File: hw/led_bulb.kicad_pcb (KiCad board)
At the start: 2 copper layers, 92.4 x 91.4 mm, 109 parts, among them P1 USB_OTG, P10 CONN_01X02, P11 CONN_01X02, P12 CONN_01X02, P13 CONN_01X02, P14 CONN_01X02, P15 CONN_01X02, P16 CONN_01X02, P17 CONN_01X02, P18 CONN_01X02, P19 CONN_01X02, P2 CONN_01X02, P20 CONN_01X02, P21 CONN_01X02, P22 CONN_01X02, P23 CONN_01X02, P24 CONN_01X02, P25 CONN_01X02, P26 CONN_01X02, P27 CONN_01X02, P28 CONN_01X02, P29 CONN_01X02, P3 CONN_01X02, P30 CONN_01X02, P31 CONN_01X02, P32 CONN_01X02, P33 CONN_01X02, P4 CONN_01X02, P5 CONN_01X02, P6 CONN_01X02, P7 CONN_01X02, P8 CONN_01X02, P9 CONN_01X02, SW1 SW_RST, SW2 SW_FLASH, U1 CP2102, U3 ESP-12E, U4 AP1117D33

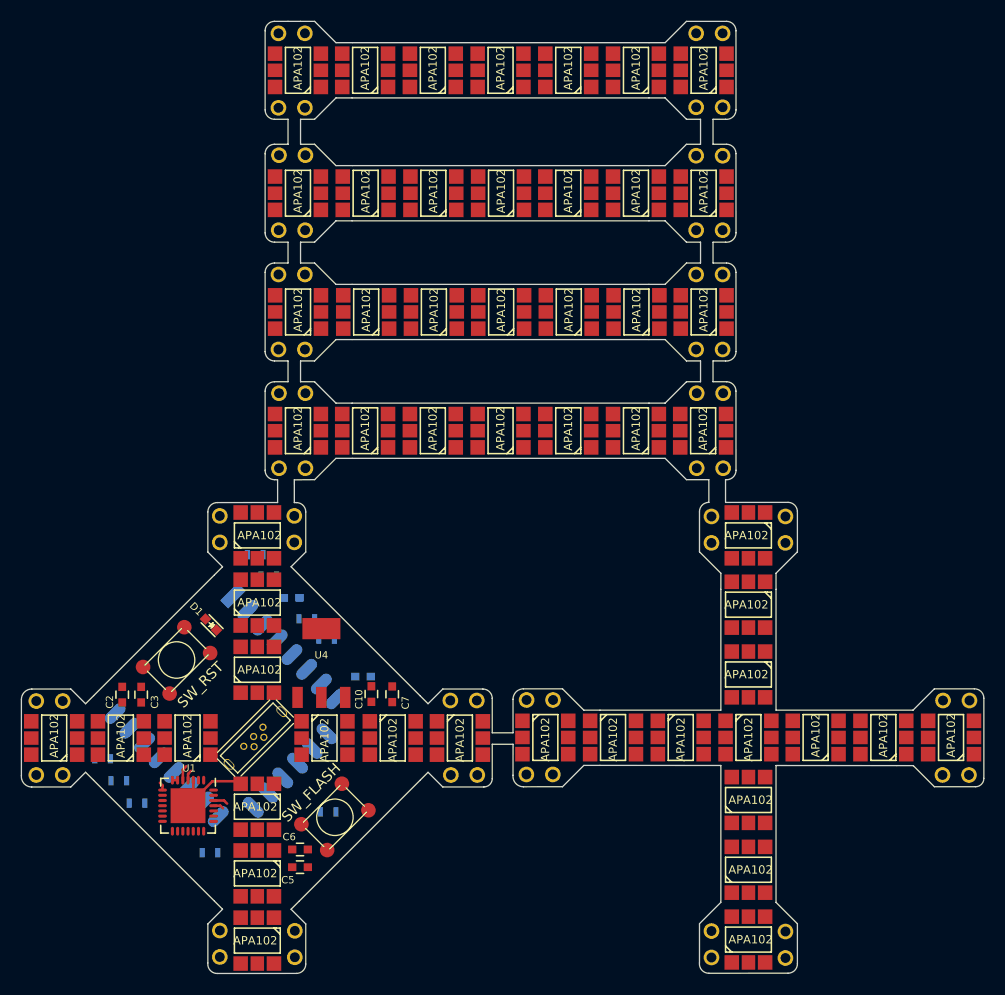
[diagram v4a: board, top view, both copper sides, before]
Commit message: Imported traces and added mouse-bite holes.
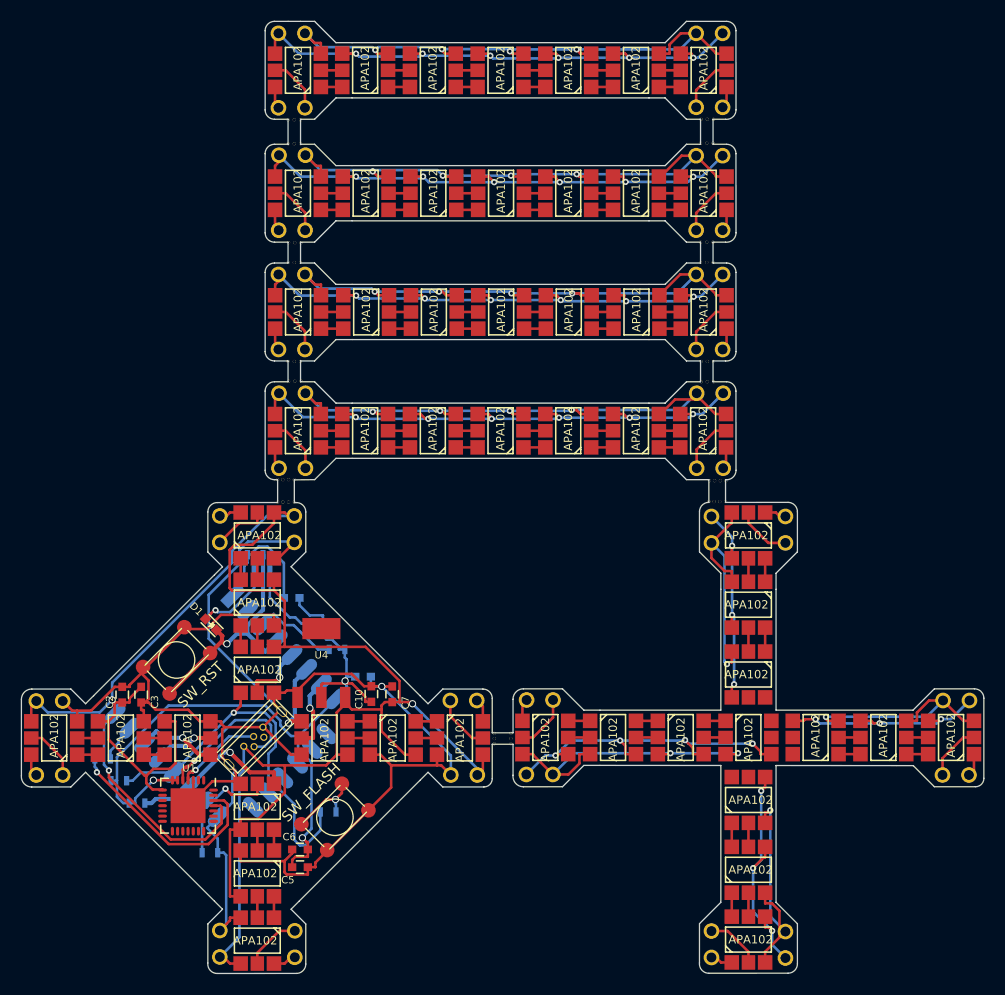
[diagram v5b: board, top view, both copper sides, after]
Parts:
- added HOLE0: 0.3mm, footprints:0.3mm, F.Cu at (130.1, 145.7)
- added HOLE0: 0.3mm, footprints:0.3mm, F.Cu at (109.8, 109.5)
- added HOLE0: 0.3mm, footprints:0.3mm, F.Cu at (108.7, 109.5)
- added HOLE0: 0.3mm, footprints:0.3mm, F.Cu at (109.2, 109.5)
- added HOLE0: 0.3mm, footprints:0.3mm, F.Cu at (109.8, 100.0)
- added HOLE0: 0.3mm, footprints:0.3mm, F.Cu at (108.7, 100.0)
- added HOLE0: 0.3mm, footprints:0.3mm, F.Cu at (109.2, 100.0)
- added HOLE0: 0.3mm, footprints:0.3mm, F.Cu at (109.9, 98.0)
- added HOLE0: 0.3mm, footprints:0.3mm, F.Cu at (108.7, 98.0)
- added HOLE0: 0.3mm, footprints:0.3mm, F.Cu at (109.3, 98.0)
- added HOLE0: 0.3mm, footprints:0.3mm, F.Cu at (109.8, 88.5)
- added HOLE0: 0.3mm, footprints:0.3mm, F.Cu at (130.1, 145.2)
- added HOLE0: 0.3mm, footprints:0.3mm, F.Cu at (108.7, 88.5)
- added HOLE0: 0.3mm, footprints:0.3mm, F.Cu at (109.2, 88.5)
- added HOLE0: 0.3mm, footprints:0.3mm, F.Cu at (109.8, 86.2)
- added HOLE0: 0.3mm, footprints:0.3mm, F.Cu at (108.7, 86.2)
- added HOLE0: 0.3mm, footprints:0.3mm, F.Cu at (109.2, 86.2)
- added HOLE0: 0.3mm, footprints:0.3mm, F.Cu at (149.5, 86.2)
- added HOLE0: 0.3mm, footprints:0.3mm, F.Cu at (148.3, 86.2)
- added HOLE0: 0.3mm, footprints:0.3mm, F.Cu at (148.9, 86.2)
- added HOLE0: 0.3mm, footprints:0.3mm, F.Cu at (149.4, 88.5)
- added HOLE0: 0.3mm, footprints:0.3mm, F.Cu at (148.2, 88.5)
- added HOLE0: 0.3mm, footprints:0.3mm, F.Cu at (130.1, 146.2)
- added HOLE0: 0.3mm, footprints:0.3mm, F.Cu at (148.8, 88.5)
- added HOLE0: 0.3mm, footprints:0.3mm, F.Cu at (149.4, 98.0)
- added HOLE0: 0.3mm, footprints:0.3mm, F.Cu at (148.2, 98.0)
- added HOLE0: 0.3mm, footprints:0.3mm, F.Cu at (148.8, 98.0)
- added HOLE0: 0.3mm, footprints:0.3mm, F.Cu at (149.4, 100.0)
- added HOLE0: 0.3mm, footprints:0.3mm, F.Cu at (148.2, 100.0)
- added HOLE0: 0.3mm, footprints:0.3mm, F.Cu at (148.8, 100.0)
- added HOLE0: 0.3mm, footprints:0.3mm, F.Cu at (149.5, 109.5)
- added HOLE0: 0.3mm, footprints:0.3mm, F.Cu at (148.3, 109.5)
- added HOLE0: 0.3mm, footprints:0.3mm, F.Cu at (148.9, 109.5)
- added HOLE0: 0.3mm, footprints:0.3mm, F.Cu at (128.4, 145.7)
- added HOLE0: 0.3mm, footprints:0.3mm, F.Cu at (149.6, 120.9)
- added HOLE0: 0.3mm, footprints:0.3mm, F.Cu at (150.2, 120.9)
- added HOLE0: 0.3mm, footprints:0.3mm, F.Cu at (149.1, 120.9)
- added HOLE0: 0.3mm, footprints:0.3mm, F.Cu at (150.7, 120.9)
- added HOLE0: 0.3mm, footprints:0.3mm, F.Cu at (149.1, 122.9)
- added HOLE0: 0.3mm, footprints:0.3mm, F.Cu at (150.1, 122.9)
- added HOLE0: 0.3mm, footprints:0.3mm, F.Cu at (149.6, 122.9)
- added HOLE0: 0.3mm, footprints:0.3mm, F.Cu at (150.7, 122.9)
- added HOLE0: 0.3mm, footprints:0.3mm, F.Cu at (108.7, 120.8)
- added HOLE0: 0.3mm, footprints:0.3mm, F.Cu at (109.2, 120.8)
- added HOLE0: 0.3mm, footprints:0.3mm, F.Cu at (128.4, 145.2)
- added HOLE0: 0.3mm, footprints:0.3mm, F.Cu at (108.2, 120.8)
- added HOLE0: 0.3mm, footprints:0.3mm, F.Cu at (107.7, 120.8)
- added HOLE0: 0.3mm, footprints:0.3mm, F.Cu at (109.2, 123.0)
- added HOLE0: 0.3mm, footprints:0.3mm, F.Cu at (108.7, 123.0)
- added HOLE0: 0.3mm, footprints:0.3mm, F.Cu at (108.2, 123.0)
- added HOLE0: 0.3mm, footprints:0.3mm, F.Cu at (107.7, 123.0)
- added HOLE0: 0.3mm, footprints:0.3mm, F.Cu at (149.5, 111.4)
- added HOLE0: 0.3mm, footprints:0.3mm, F.Cu at (148.9, 111.4)
- added HOLE0: 0.3mm, footprints:0.3mm, F.Cu at (148.3, 111.4)
- added HOLE0: 0.3mm, footprints:0.3mm, F.Cu at (128.4, 146.2)
- added HOLE0: 0.3mm, footprints:0.3mm, F.Cu at (109.9, 111.3)
- added HOLE0: 0.3mm, footprints:0.3mm, F.Cu at (108.7, 111.3)
- added HOLE0: 0.3mm, footprints:0.3mm, F.Cu at (109.3, 111.3)
- moved R3 1.41 mm to (113.3, 137.1)
- moved R4 0.92 mm to (111.2, 134.6)
- moved R6 0.88 mm to (106.2, 129.4)
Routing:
- net V_USB: track 0.80 -> 183.0 mm, vias 0 -> 2
- net GND: track 15.4 -> 185.3 mm, vias 0 -> 1
- net V_3.3: track 0.50 -> 78.6 mm, vias 0 -> 3
- net Net-(LED13-Pad3): track 0.00 -> 56.9 mm, vias 0 -> 4
- net Net-(LED16-Pad3): track 0.00 -> 56.8 mm, vias 0 -> 4
- net Net-(LED15-Pad3): track 0.00 -> 56.8 mm, vias 0 -> 4
- net Net-(LED14-Pad3): track 0.00 -> 56.4 mm, vias 0 -> 4
- net Net-(LED16-Pad4): track 0.00 -> 56.3 mm, vias 0 -> 6
- net Net-(LED14-Pad4): track 0.00 -> 55.9 mm, vias 0 -> 6
- net Net-(LED15-Pad4): track 0.00 -> 55.8 mm, vias 0 -> 6
- net Net-(LED13-Pad4): track 0.00 -> 55.5 mm, vias 0 -> 6
- net GPIO0: track 0.00 -> 37.3 mm, vias 0 -> 1
- net Net-(LED41-Pad4): track 0.00 -> 32.1 mm, vias 0 -> 4
- net Net-(LED41-Pad3): track 0.00 -> 29.8 mm, vias 0 -> 2
- net Net-(LED44-Pad4): track 0.00 -> 23.6 mm, vias 0 -> 3
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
